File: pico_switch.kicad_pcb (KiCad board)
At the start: 2 copper layers, 88.9 x 52.1 mm, 26 parts, among them J1 Conn_01x09_Female_pico, J2 Conn_01x09_Female_pico, J3 Conn_01x04_Female, J4 Conn_01x09_Female_pico, J5 Conn_01x09_Female_pico, J6 Conn_01x04_Female, U1 pico, U2 HC_SR04, U3 usb_to_ttl, U4 step_up_5v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

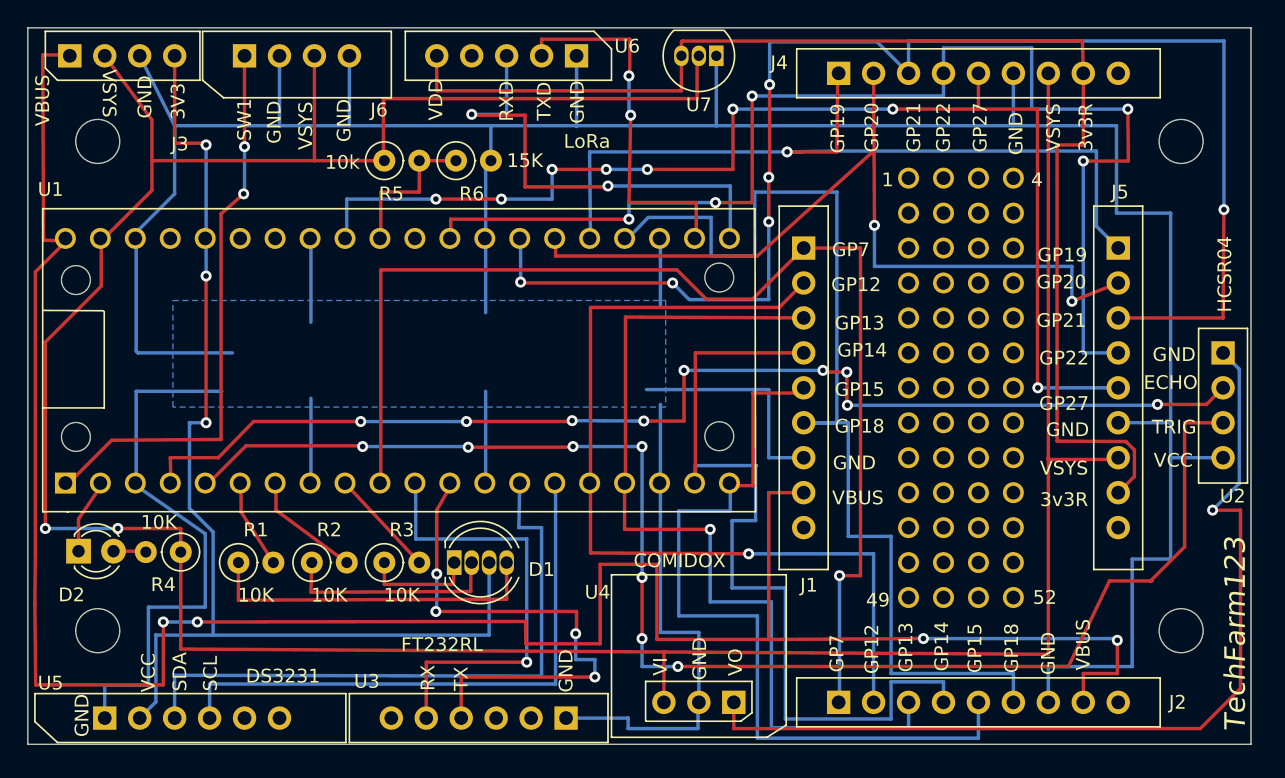
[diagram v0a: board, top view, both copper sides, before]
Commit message: PCB fixes/cleanup and getting it ready for AllPCP fabrication
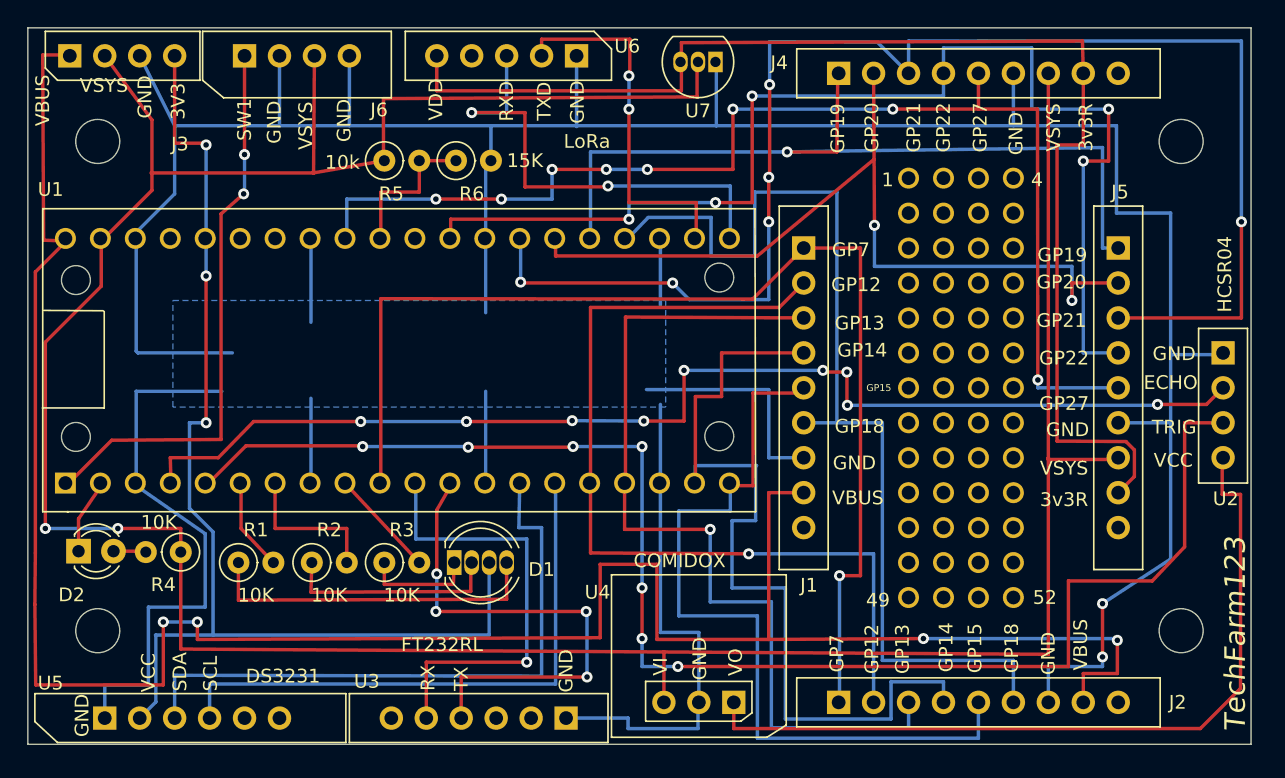
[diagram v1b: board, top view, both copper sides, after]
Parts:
- moved U7 0.45 mm to (125.7, 62.7)
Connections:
- U2 pad 1: Net-(U2-Pad1) -> GND
- U2 pad 4: GND -> Net-(U2-Pad4)
- U4 pad 1: Net-(U2-Pad1) -> Net-(U2-Pad4)
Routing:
- net Net-(U2-Pad1): track 67.6 -> 0.00 mm, vias 1 -> 0
- net Net-(U2-Pad4): track 0.00 -> 58.1 mm
- net Net-(J1-Pad1): track 87.5 -> 84.6 mm
- net Net-(R2-Pad2): track 8.18 -> 11.0 mm
- net Net-(J4-Pad4): track 91.4 -> 88.6 mm
- net Net-(J4-Pad3): track 104.4 -> 107.1 mm
- net Net-(J1-Pad6): track 78.3 -> 75.8 mm
- net Net-(U1-Pad5): track 105.4 -> 107.6 mm
- net Net-(J4-Pad2): track 61.7 -> 63.5 mm
- net GND: track 316.0 -> 314.2 mm, vias 0 -> 2
- net Net-(U1-Pad12): track 38.5 -> 37.3 mm
- net Net-(J4-Pad1): track 60.4 -> 61.5 mm
- net VBUS: track 166.2 -> 165.5 mm
- net VSYS: track 226.7 -> 227.4 mm

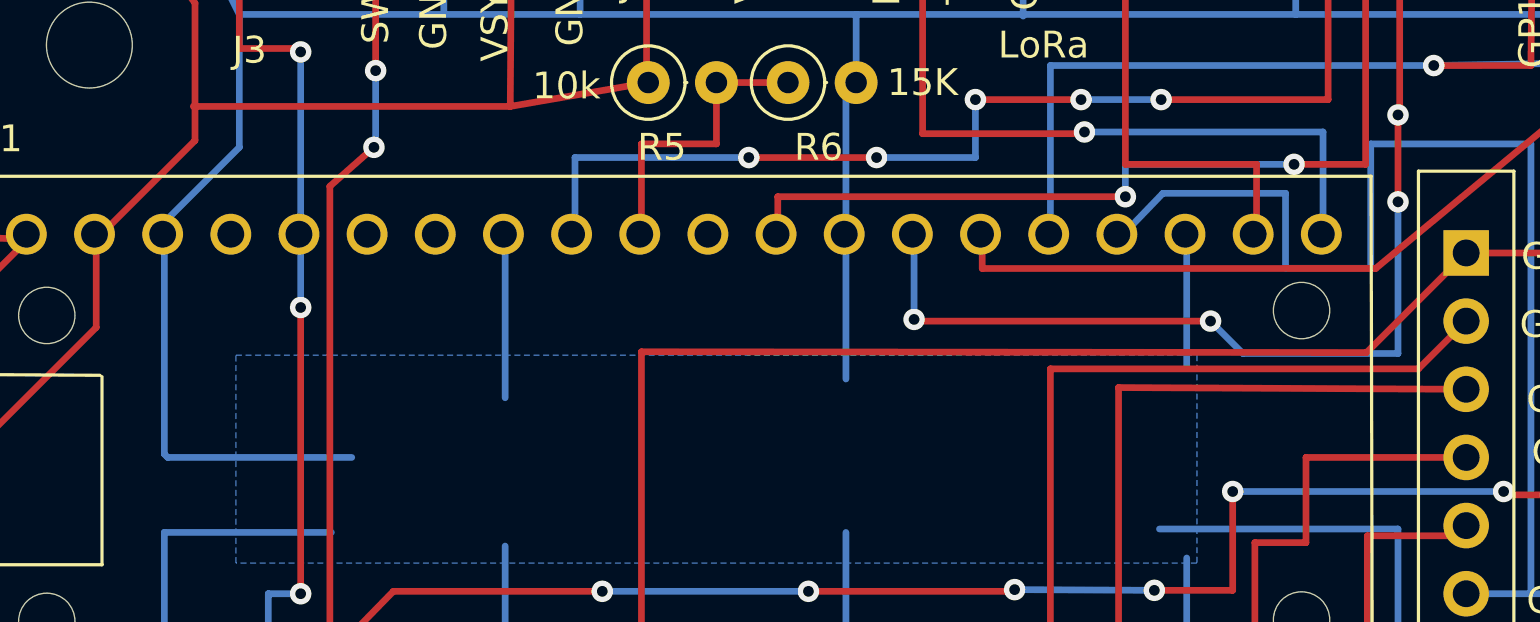
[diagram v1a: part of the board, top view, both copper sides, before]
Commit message: trace/vias tweaking for spacing mostly
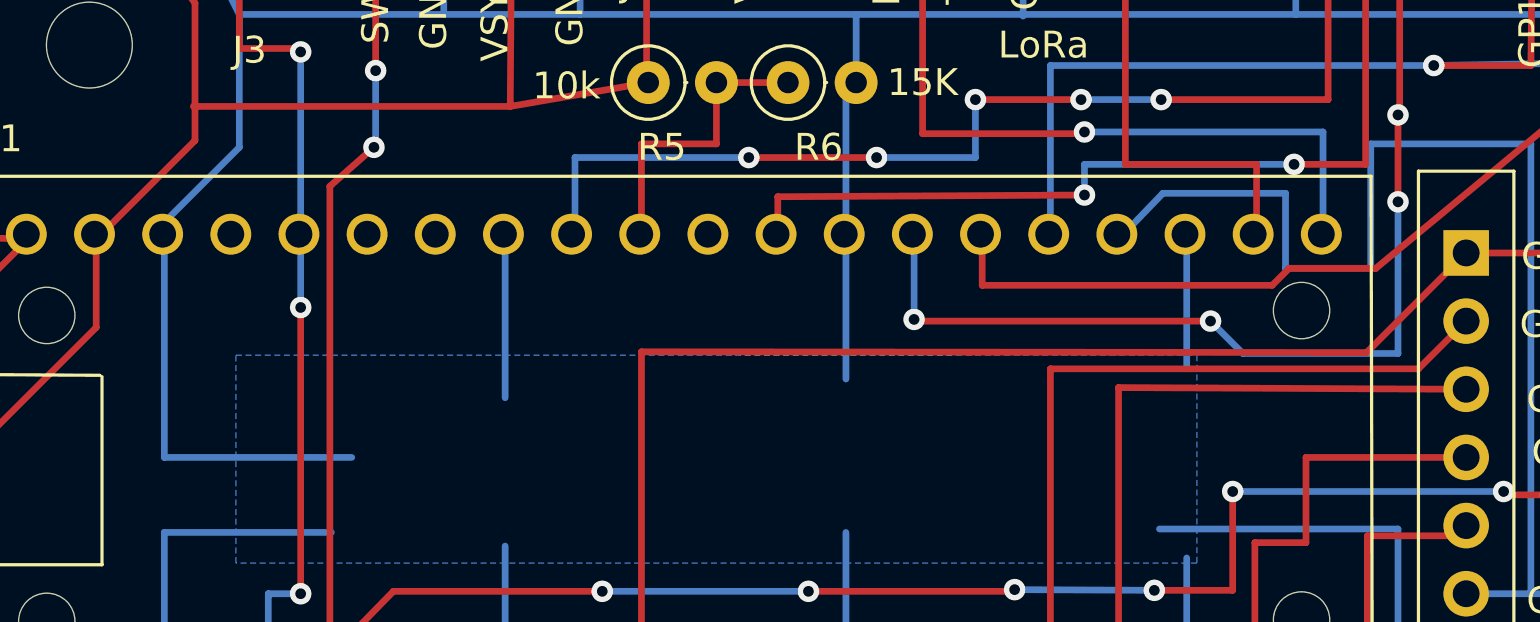
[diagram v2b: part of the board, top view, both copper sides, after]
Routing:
- net Net-(J4-Pad2): track 63.5 -> 64.4 mm
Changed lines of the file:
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@@
     (thickness 1.6)
     (drawings 73)
-    (tracks 451)
+    (tracks 452)
     (zones 0)
     (modules 26)
@@
   (page A4)
   (layers
-    (0 F.Cu signal)
+    (0 F.Cu signal hide)
     (31 B.Cu signal)
     (32 B.Adhes user)
@@
     (pad_to_mask_clearance 0)
     (aux_axis_origin 0 0)
-    (visible_elements 7FFFFFFF)
+    (visible_elements 7FFFF7FF)
     (pcbplotparams
       (layerselection 0x010fc_ffffffff)
@@
   (gr_line (start 164.592 112.268) (end 75.692 112.268) (layer Edge.Cuts) (width 0.05))
   (gr_line (start 75.692 112.268) (end 75.692 60.198) (layer Edge.Cuts) (width 0.05))
-  (via (at 153.797 102.0445) (size 0.8) (drill 0.4) (layers F.Cu B.Cu) (net 4))
   (segment (start 107.88099 99.12901) (end 107.95 99.06) (width 0.25) (layer F.Cu) (net 1))
   (segment (start 107.88099 101.16101) (end 107.8865 99.07102) (width 0.25) (layer F.Cu) (net 1))
@@
   (segment (start 96.4565 70.739) (end 101.6 69.85) (width 0.25) (layer F.Cu) (net 3))
   (segment (start 96.52 62.23) (end 96.4565 70.739) (width 0.25) (layer F.Cu) (net 3))
+  (via (at 153.797 102.0445) (size 0.8) (drill 0.4) (layers F.Cu B.Cu) (net 4))
   (segment (start 93.98 62.23) (end 93.98 67.31) (width 0.25) (layer B.Cu) (net 4))
   (segment (start 108.966 75.692) (end 108.966 80.899) (width 0.25) (layer B.Cu) (net 4))
@@
   (segment (start 125.73 67.31) (end 86.36 67.31) (width 0.25) (layer B.Cu) (net 4))
   (segment (start 115.57 62.23) (end 115.57 67.3735) (width 0.25) (layer B.Cu) (net 4))
-  (segment (start 83.693 83.82) (end 90.551 83.82) (width 0.25) (layer B.Cu) (net 4))
-  (segment (start 83.566 83.693) (end 83.693 83.82) (width 0.25) (layer B.Cu) (net 4))
-  (segment (start 83.566 75.057) (end 83.566 83.693) (width 0.25) (layer B.Cu) (net 4))
-  (segment (start 86.36 72.263) (end 83.566 75.057) (width 0.25) (layer B.Cu) (net 4))
-  (segment (start 86.36 67.31) (end 86.36 72.263) (width 0.25) (layer B.Cu) (net 4))
   (segment (start 83.82 62.23) (end 86.36 67.31) (width 0.25) (layer B.Cu) (net 4))
   (segment (start 83.566 86.614) (end 89.789 86.614) (width 0.25) (layer B.Cu) (net 4))
@@
   (segment (start 153.797 102.0445) (end 158.75 98.806) (width 0.25) (layer B.Cu) (net 4))
   (segment (start 153.797 105.918) (end 153.797 102.0445) (width 0.25) (layer F.Cu) (net 4))
+  (segment (start 83.566 75.057) (end 83.566 83.82) (width 0.25) (layer B.Cu) (net 4))
+  (segment (start 86.36 72.263) (end 83.566 75.057) (width 0.25) (layer B.Cu) (net 4))
+  (segment (start 86.36 67.31) (end 86.36 72.263) (width 0.25) (layer B.Cu) (net 4))
+  (segment (start 83.566 83.82) (end 90.551 83.82) (width 0.25) (layer B.Cu) (net 4))
   (segment (start 98.8695 96.5835) (end 98.8695 99.06) (width 0.25) (layer F.Cu) (net 8))
   (segment (start 93.6625 93.2815) (end 93.6625 96.5835) (width 0.25) (layer F.Cu) (net 8))
@@
   (via (at 128.3335 65.151) (size 0.8) (drill 0.4) (layers F.Cu B.Cu) (net 31))
   (segment (start 142.24 65.151) (end 128.3335 65.151) (width 0.25) (layer B.Cu) (net 31))
-  (via (at 119.38 74.1045) (size 0.8) (drill 0.4) (layers F.Cu B.Cu) (net 31))
+  (via (at 117.856 74.041) (size 0.8) (drill 0.4) (layers F.Cu B.Cu) (net 31))
   (via (at 125.6665 72.898) (size 0.8) (drill 0.4) (layers F.Cu B.Cu) (net 31))
-  (segment (start 119.38 72.898) (end 125.6665 72.898) (width 0.25) (layer B.Cu) (net 31))
-  (segment (start 119.38 74.1045) (end 119.38 72.898) (width 0.25) (layer B.Cu) (net 31))
   (segment (start 128.3335 65.151) (end 128.3335 72.898) (width 0.25) (layer F.Cu) (net 31))
   (segment (start 125.6665 72.898) (end 128.3335 72.898) (width 0.25) (layer F.Cu) (net 31))
-  (segment (start 106.426 74.1045) (end 119.38 74.1045) (width 0.25) (layer F.Cu) (net 31))
-  (segment (start 106.426 75.692) (end 106.426 74.1045) (width 0.25) (layer F.Cu) (net 31))
   (via (at 152.4 69.8765) (size 0.8) (drill 0.4) (layers F.Cu B.Cu) (net 31))
   (segment (start 154.94 83.82) (end 152.4 83.82) (width 0.25) (layer B.Cu) (net 31))
@@
   (segment (start 148.6535 66.1035) (end 148.6535 61.6585) (width 0.25) (layer B.Cu) (net 31))
   (segment (start 154.2415 66.1035) (end 148.6535 66.1035) (width 0.25) (layer B.Cu) (net 31))
+  (segment (start 106.426 74.1045) (end 117.856 74.041) (width 0.25) (layer F.Cu) (net 31))
+  (segment (start 106.426 75.692) (end 106.426 74.1045) (width 0.25) (layer F.Cu) (net 31))
+  (segment (start 117.856 72.898) (end 125.6665 72.898) (width 0.25) (layer B.Cu) (net 31))
+  (segment (start 117.856 74.041) (end 117.856 72.898) (width 0.25) (layer B.Cu) (net 31))
   (via (at 163.8935 74.295) (size 0.8) (drill 0.4) (layers F.Cu B.Cu) (net 32))
   (segment (start 139.7 63.5) (end 137.414 61.214) (width 0.25) (layer B.Cu) (net 32))
@@
   (segment (start 137.2235 74.549) (end 137.16 63.5) (width 0.25) (layer F.Cu) (net 33))
   (segment (start 154.94 78.74) (end 151.5745 78.74) (width 0.25) (layer F.Cu) (net 33))
-  (segment (start 114.046 76.779001) (end 114.046 75.692) (width 0.25) (layer F.Cu) (net 33))
-  (segment (start 128.706999 76.779001) (end 114.046 76.779001) (width 0.25) (layer F.Cu) (net 33))
-  (segment (start 137.195923 69.750577) (end 128.706999 76.779001) (width 0.25) (layer F.Cu) (net 33))
   (segment (start 137.2235 77.5335) (end 137.2235 74.549) (width 0.25) (layer B.Cu) (net 33))
   (segment (start 151.5745 77.5335) (end 137.2235 77.5335) (width 0.25) (layer B.Cu) (net 33))
@@
   (segment (start 151.5745 78.74) (end 151.5745 80.01) (width 0.25) (layer B.Cu) (net 33))
   (segment (start 151.5745 78.74) (end 151.5745 80.01) (width 0.25) (layer F.Cu) (net 33))
+  (segment (start 114.046 77.4065) (end 114.046 75.692) (width 0.25) (layer F.Cu) (net 33))
+  (segment (start 137.195923 69.750577) (end 128.706999 76.779001) (width 0.25) (layer F.Cu) (net 33))
+  (segment (start 125.478197 76.779001) (end 128.706999 76.779001) (width 0.25) (layer F.Cu) (net 33))
+  (segment (start 124.850698 77.4065) (end 125.478197 76.779001) (width 0.25) (layer F.Cu) (net 33))
+  (segment (start 114.046 77.4065) (end 124.850698 77.4065) (width 0.25) (layer F.Cu) (net 33))
   (via (at 130.8735 69.215) (size 0.8) (drill 0.4) (layers F.Cu B.Cu) (net 34))
   (segment (start 134.5565 63.5635) (end 134.62 63.5) (width 0.25) (layer F.Cu) (net 34))
